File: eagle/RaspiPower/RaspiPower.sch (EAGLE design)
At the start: 31 parts, among them K1 4052

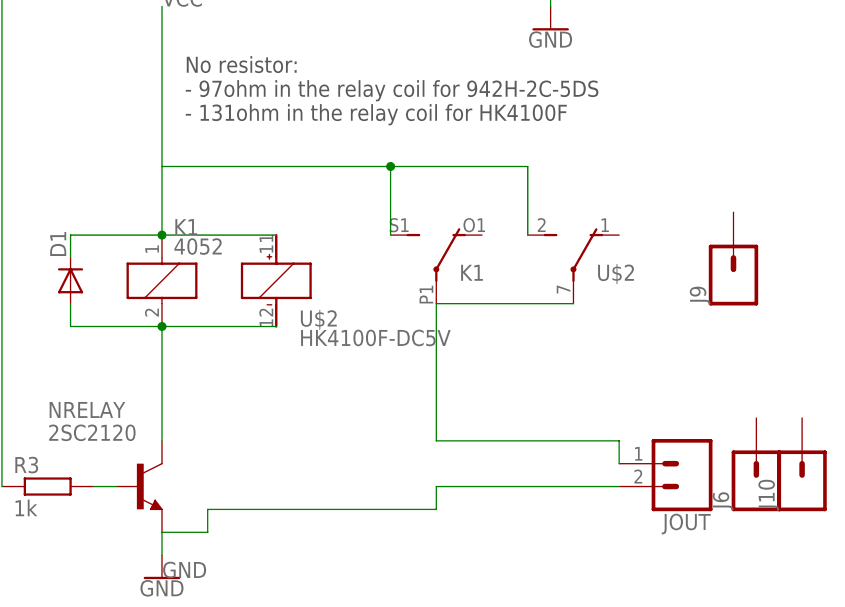
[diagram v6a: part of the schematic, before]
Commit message: Added HK4100F relay part to library, and v1.2 of the RaspiPower
Conclusion: don't use other third party parts symbols found on the net
without verifying thoroughly that their are good.
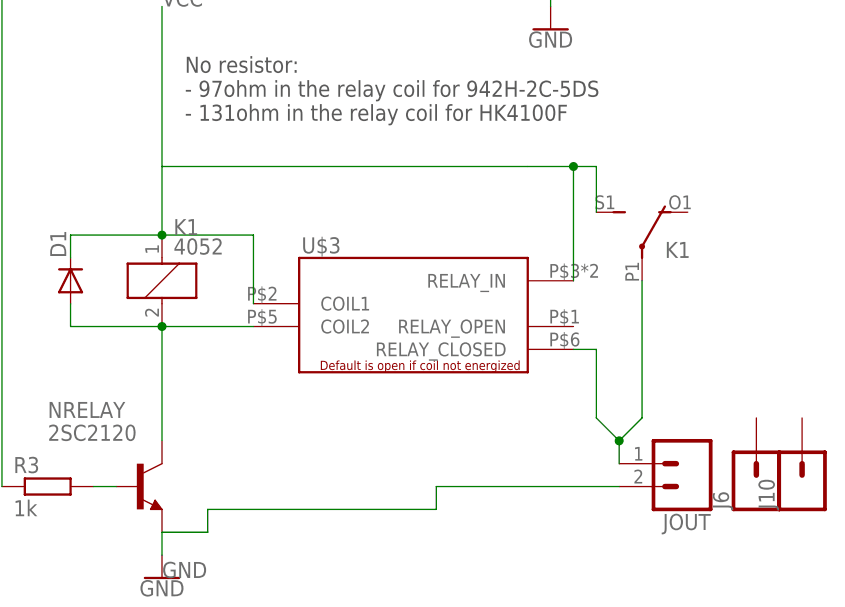
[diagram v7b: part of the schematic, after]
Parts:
- removed J9: (no value), SparkFun-Connectors:CONN_01PTH_NO_SILK_YES_STOP
- removed U$2: HK4100F-DC5V, huike:HK4100F-DC5V
- added U$3: HK4100F, kalshagar:HK4100F
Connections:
- removed net N$3: JOUT.1, K12.P, U$2G$2.P
- new net VOUT: JOUT.1, K12.P, U$3.RELAY_CLOSED
- net N$9: now also U$3.COIL2; no longer U$2G$1.-
- net VCC: now also U$3.COIL1, U$3.RELAY_IN; no longer U$2G$1.+, U$2G$2.S
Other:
- moved on the sheet: K1
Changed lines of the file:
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@@
 <part name="J2" library="SparkFun-Connectors" deviceset="CONN_05X2" device="PTH"/>
 <part name="JSPIPROG" library="SparkFun-Connectors" deviceset="AVR_SPI_PROG_3X2" device="PTH"/>
-<part name="U$2" library="huike" deviceset="HK410?F-*" device="0" technology="DC5V"/>
 <part name="JOUT" library="SparkFun-Connectors" deviceset="CONN_02" device="LOCK_LONGPADS"/>
 <part name="JIN" library="SparkFun-Connectors" deviceset="CONN_02" device="LOCK_LONGPADS"/>
 <part name="J7" library="SparkFun-Connectors" deviceset="CONN_05X2" device="PTH"/>
 <part name="J8" library="SparkFun-Connectors" deviceset="CONN_05X2" device="PTH"/>
-<part name="J9" library="SparkFun-Connectors" deviceset="CONN_01" device="PTH_NO_SILK_YES_STOP"/>
 <part name="GND4" library="SparkFun-PowerSymbols" deviceset="GND" device=""/>
 <part name="R6" library="resistor" deviceset="R-EU_" device="R1206W" value="1k"/>
@@
 <part name="S1" library="SparkFun-Switches" deviceset="MOMENTARY-SWITCH-SPST" device="-PTH-6.0MM"/>
 <part name="C1" library="resistor" deviceset="CPOL-EU" device="E2.5-5" value="10uF"/>
+<part name="U$3" library="kalshagar" deviceset="HK4100F" device=""/>
 </parts>
 <sheets>
@@
 <instance part="NRELAY" gate="G$1" x="83.82" y="-35.56"/>
 <instance part="K1" gate="1" x="86.36" y="-12.7"/>
-<instance part="K1" gate="2" x="116.84" y="-12.7"/>
+<instance part="K1" gate="2" x="139.7" y="-10.16"/>
 <instance part="R3" gate="G$1" x="73.66" y="-35.56"/>
 <instance part="D1" gate="G$1" x="76.2" y="-12.7" rot="R90"/>
@@
 <instance part="J2" gate="G$1" x="134.62" y="83.82"/>
 <instance part="JSPIPROG" gate="G$1" x="91.44" y="149.86"/>
-<instance part="U$2" gate="G$1" x="99.06" y="-12.7"/>
-<instance part="U$2" gate="G$2" x="132.08" y="-12.7"/>
 <instance part="JOUT" gate="G$1" x="144.78" y="-33.02" rot="R180"/>
 <instance part="JIN" gate="G$1" x="-15.24" y="129.54"/>
 <instance part="J7" gate="G$1" x="134.62" y="101.6"/>
 <instance part="J8" gate="G$1" x="134.62" y="119.38"/>
-<instance part="J9" gate="G$1" x="149.86" y="-12.7" rot="R90"/>
 <instance part="GND4" gate="1" x="86.36" y="-45.72"/>
 <instance part="R6" gate="G$1" x="25.4" y="-7.62" rot="R90"/>
@@
 <instance part="S1" gate="G$1" x="50.8" y="33.02" rot="R180"/>
 <instance part="C1" gate="G$1" x="-27.94" y="132.08"/>
+<instance part="U$3" gate="G$1" x="119.38" y="-33.02"/>
 </instances>
 <busses>
@@
 <pinref part="K1" gate="1" pin="1"/>
 <pinref part="D1" gate="G$1" pin="C"/>
-<wire x1="86.36" y1="0" x2="111.76" y2="0" width="0.1524" layer="91"/>
-<pinref part="U$2" gate="G$1" pin="+"/>
-<wire x1="111.76" y1="0" x2="127" y2="0" width="0.1524" layer="91"/>
-<wire x1="86.36" y1="-7.62" x2="99.06" y2="-7.62" width="0.1524" layer="91"/>
+<wire x1="86.36" y1="0" x2="127" y2="0" width="0.1524" layer="91"/>
 <pinref part="K1" gate="2" pin="S"/>
-<wire x1="111.76" y1="-7.62" x2="111.76" y2="0" width="0.1524" layer="91"/>
-<junction x="111.76" y="0"/>
-<pinref part="U$2" gate="G$2" pin="S"/>
-<wire x1="127" y1="0" x2="127" y2="-7.62" width="0.1524" layer="91"/>
+<wire x1="132.08" y1="0" x2="134.62" y2="0" width="0.1524" layer="91"/>
+<wire x1="134.62" y1="-5.08" x2="134.62" y2="0" width="0.1524" layer="91"/>
+<pinref part="U$3" gate="G$1" pin="COIL1"/>
+<wire x1="86.36" y1="-7.62" x2="96.52" y2="-7.62" width="0.1524" layer="91"/>
+<wire x1="96.52" y1="-7.62" x2="96.52" y2="-15.24" width="0.1524" layer="91"/>
+<pinref part="U$3" gate="G$1" pin="RELAY_IN"/>
+<wire x1="127" y1="0" x2="132.08" y2="0" width="0.1524" layer="91"/>
+<wire x1="132.08" y1="0" x2="132.08" y2="-12.7" width="0.1524" layer="91"/>
+<junction x="132.08" y="0"/>
 </segment>
 <segment>
@@
 <pinref part="NRELAY" gate="G$1" pin="C"/>
 <pinref part="D1" gate="G$1" pin="A"/>
-<pinref part="U$2" gate="G$1" pin="-"/>
-<wire x1="86.36" y1="-17.78" x2="99.06" y2="-17.78" width="0.1524" layer="91"/>
-</segment>
-</net>
-<net name="N$3" class="0">
+<pinref part="U$3" gate="G$1" pin="COIL2"/>
+<wire x1="96.52" y1="-17.78" x2="86.36" y2="-17.78" width="0.1524" layer="91"/>
+</segment>
+</net>
+<net name="VOUT" class="0">
 <segment>
 <pinref part="K1" gate="2" pin="P"/>
-<wire x1="116.84" y1="-15.24" x2="116.84" y2="-30.48" width="0.1524" layer="91"/>
-<pinref part="U$2" gate="G$2" pin="P"/>
-<wire x1="132.08" y1="-15.24" x2="116.84" y2="-15.24" width="0.1524" layer="91"/>
+<wire x1="139.7" y1="-12.7" x2="139.7" y2="-27.94" width="0.1524" layer="91"/>
 <pinref part="JOUT" gate="G$1" pin="1"/>
-<wire x1="116.84" y1="-30.48" x2="137.16" y2="-30.48" width="0.1524" layer="91"/>
+<wire x1="139.7" y1="-27.94" x2="137.16" y2="-30.48" width="0.1524" layer="91"/>
 <wire x1="137.16" y1="-30.48" x2="137.16" y2="-33.02" width="0.1524" layer="91"/>
-</segment>
-</net>
+<pinref part="U$3" gate="G$1" pin="RELAY_CLOSED"/>
+<wire x1="132.08" y1="-20.32" x2="134.62" y2="-20.32" width="0.1524" layer="91"/>
+<wire x1="134.62" y1="-20.32" x2="134.62" y2="-27.94" width="0.1524" layer="91"/>
+<wire x1="134.62" y1="-27.94" x2="137.16" y2="-30.48" width="0.1524" layer="91"/>
+<junction x="137.16" y="-30.48"/>
+</segment>
+</net>
